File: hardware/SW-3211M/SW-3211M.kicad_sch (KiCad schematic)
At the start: 41 parts, among them J1 Conn_01x07, J2 STX-3100-5N, J3 Conn_01x03, Q1 NTF2955, Q2 DMN2041L, Q3 DMN2041L, T1 42TL004-RC, U1 LMC6482

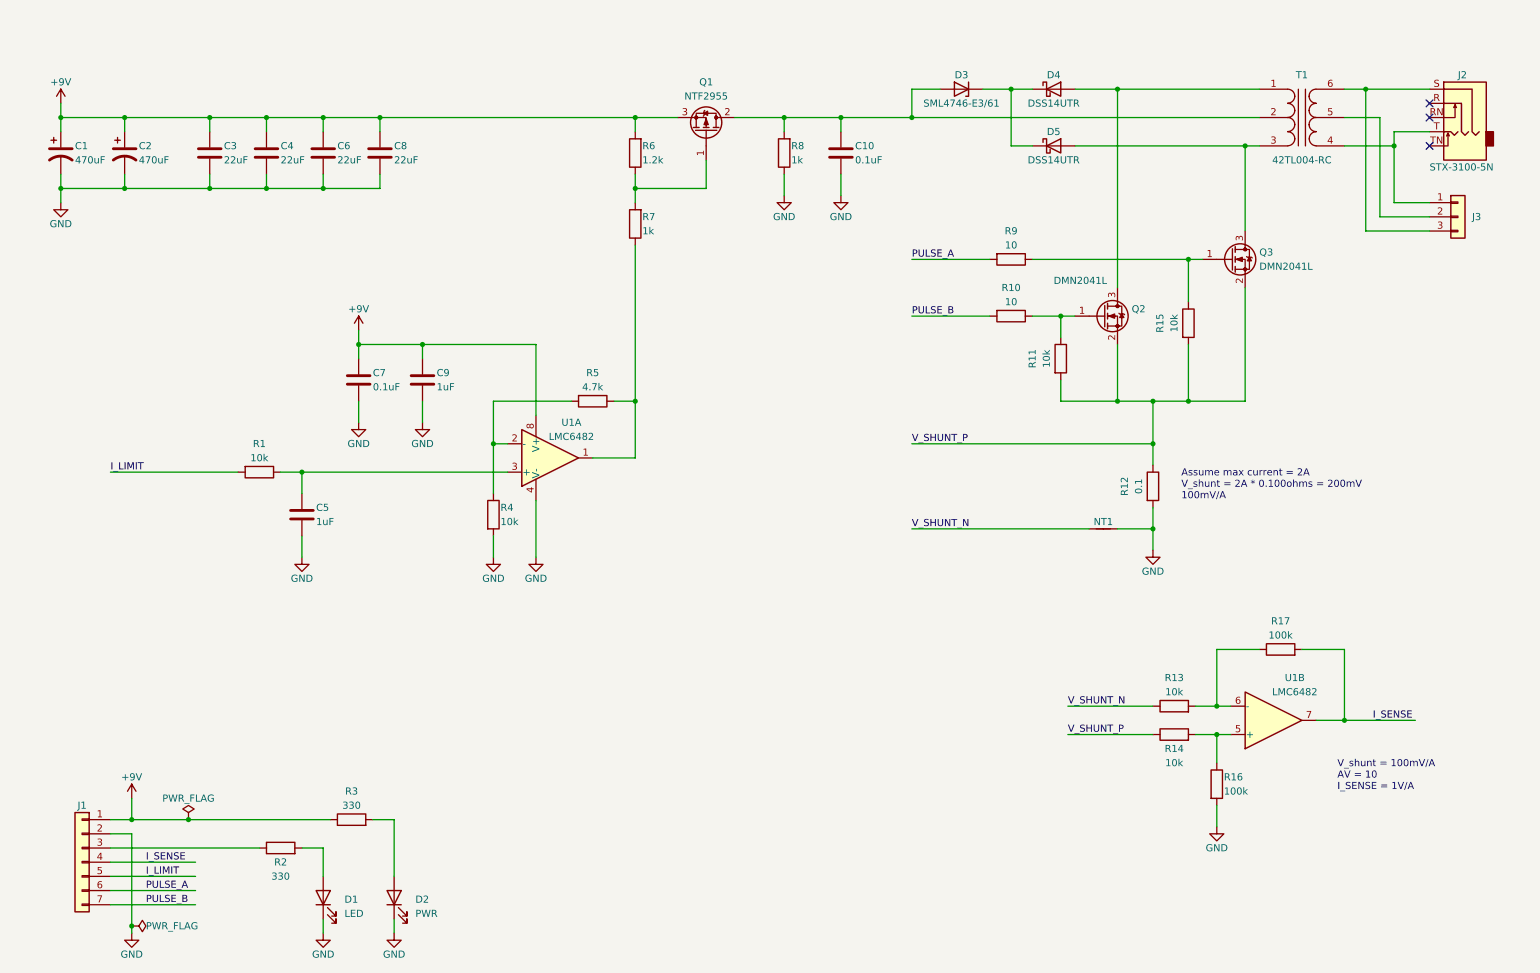
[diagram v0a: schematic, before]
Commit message: update part numbers
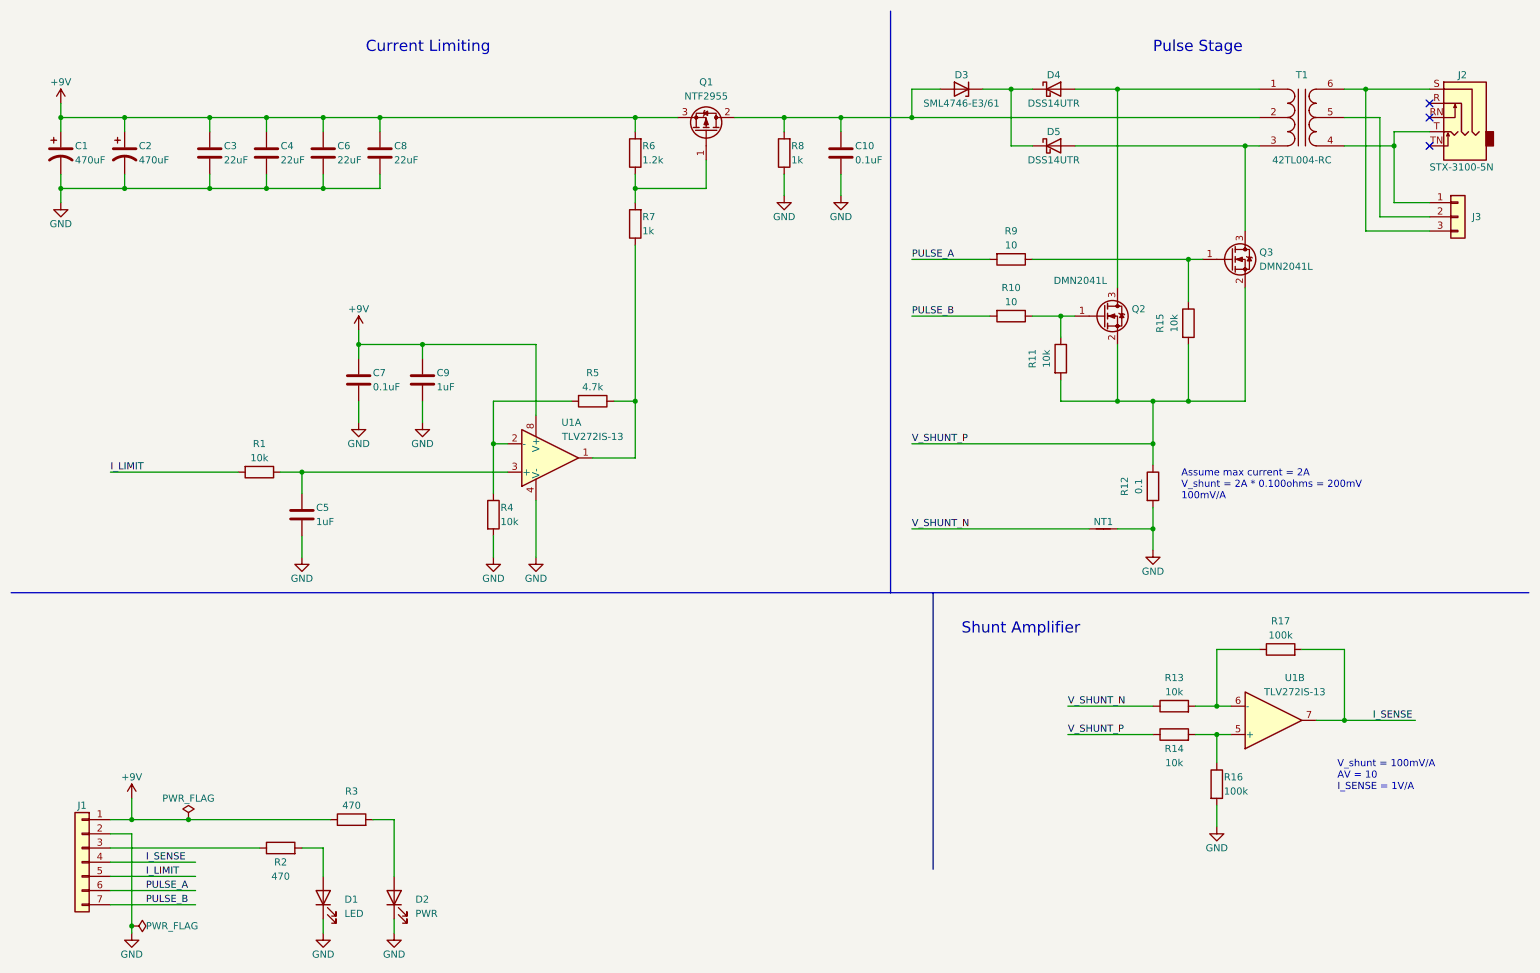
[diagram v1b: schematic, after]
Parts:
- C10, C7: MPN CL10B104KB8WPND -> CL10B104KB8NNWC
- C3, C4, C6, C8: MPN CL32A226MAJNNNE -> 12103D226MAT2A
- C5, C9: MPN CL10B105KA8NNNC -> CL10B105KA8NFNC
- D1: footprint LED_SMD:LED_0805_2012Metric -> LED_SMD:LED_0603_1608Metric; MPN (none) -> 150060VS75000
- D2: footprint LED_SMD:LED_0805_2012Metric -> LED_SMD:LED_0603_1608Metric; MPN (none) -> 150060RS75000
- R1, R11, R13, R14, R15, R4: MPN AC0603FR-1010KL -> RC0603FR-0710KL
- R16, R17: MPN CRCW0603100KFKEAC -> RC0603FR-07100KL
- R2, R3: value 330 -> 470; MPN (none) -> RC0603FR-07470RL
- R5: MPN AC0603FR-134K7L -> RC0603FR-074K7L
- R6: MPN AC0603FR-071K2L -> RC0603FR-071K2L
- U1: value LMC6482 -> TLV272IS-13; MPN LMC6482IDT -> TLV272IS-13
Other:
- note added: "Current Limiting"
- note added: "Pulse Stage"
- note added: "Shunt Amplifier"
